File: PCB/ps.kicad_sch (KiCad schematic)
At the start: 8 parts, among them J2 Power

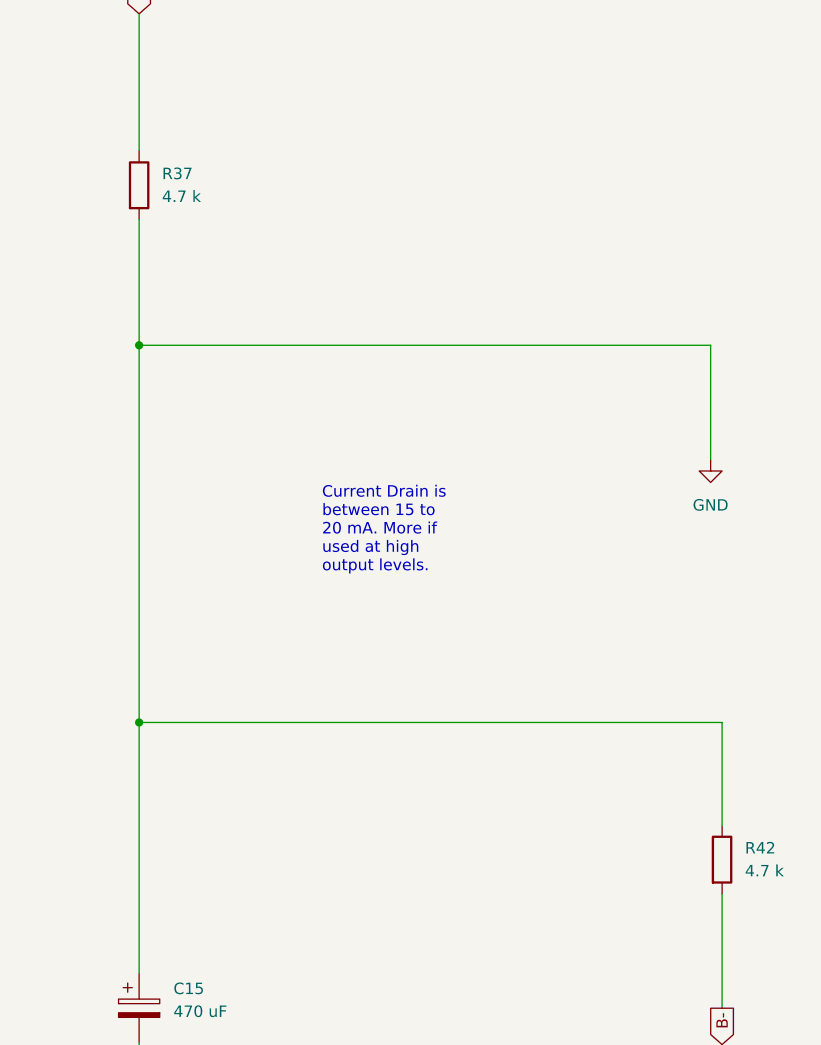
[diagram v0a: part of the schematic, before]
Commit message: Change TO-92 transistors to wide package to avoid shorting during soldering
Added B- hole for speaker
Added more vias to shorten traces
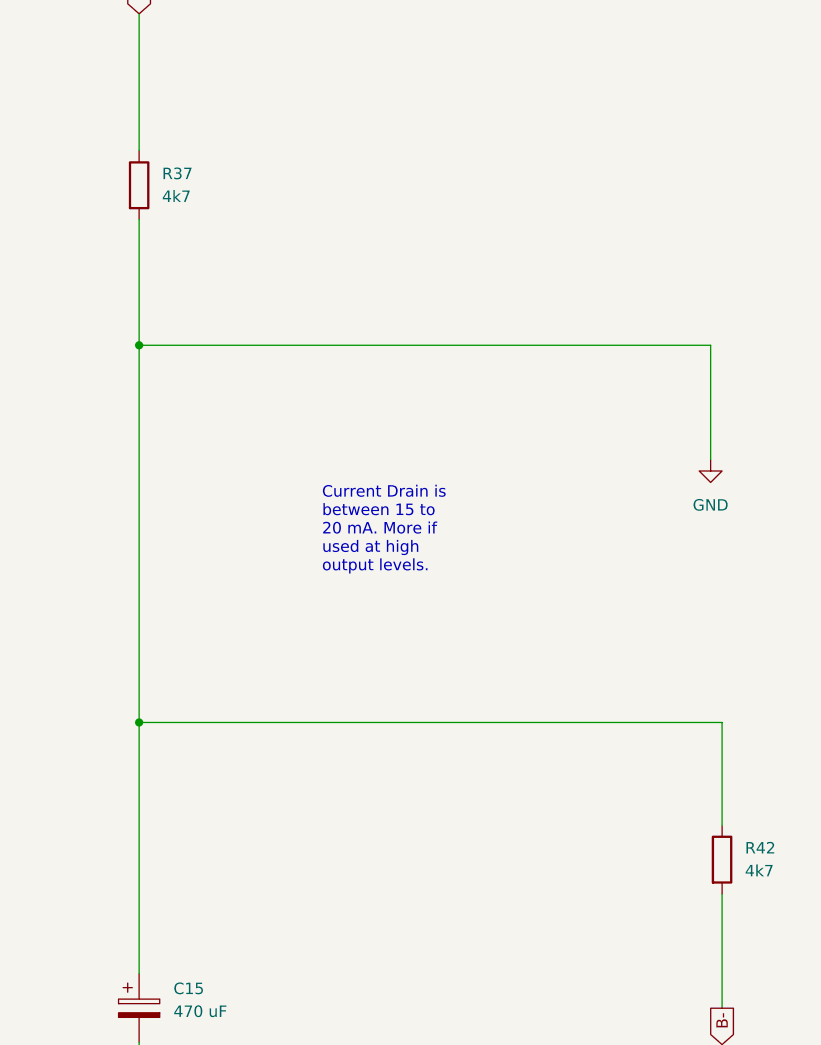
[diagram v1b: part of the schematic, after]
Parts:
- R37, R42: value 4.7 k -> 4k7
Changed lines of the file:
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@@
 		(fields_autoplaced yes)
 		(property "Reference" "R42"
-			(at 227.33 119.38 0)
-			(show_name no)
-			(do_not_autoplace no)
-			(effects
-				(font
-					(size 1.27 1.27)
-				)
-				(justify left)
-			)
-		)
-		(property "Value" "4.7 k"
-			(at 227.33 121.92 0)
+			(at 227.33 119.3799 0)
+			(show_name no)
+			(do_not_autoplace no)
+			(effects
+				(font
+					(size 1.27 1.27)
+				)
+				(justify left)
+			)
+		)
+		(property "Value" "4k7"
+			(at 227.33 121.9199 0)
 			(show_name no)
 			(do_not_autoplace no)
@@
 		(fields_autoplaced yes)
 		(property "Reference" "R37"
-			(at 162.56 44.45 0)
-			(show_name no)
-			(do_not_autoplace no)
-			(effects
-				(font
-					(size 1.27 1.27)
-				)
-				(justify left)
-			)
-		)
-		(property "Value" "4.7 k"
-			(at 162.56 46.99 0)
-			(show_name no)
-			(do_not_autoplace no)
+			(at 162.56 44.4499 0)
+			(show_name no)
+			(do_not_autoplace no)
+			(effects
+				(font
+					(size 1.27 1.27)
+				)
+				(justify left)
+			)
+		)
+		(property "Value" "4k7"
+			(at 162.56 46.9899 0)
+			(show_name no)
+			(do_not_autoplace no)

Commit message: Necessary Changes to Schematic and PCB
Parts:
- C13, C14: footprint Capacitor_THT:CP_Radial_D4.0mm_P1.50mm -> Capacitor_THT:CP_Radial_D4.0mm_P2.00mm
- C15, C23: footprint Capacitor_THT:CP_Radial_D14.0mm_P5.00mm -> Capacitor_THT:CP_Radial_D10.0mm_P5.00mm
- J10: renamed from GND1; footprint Connector_PinHeader_2.00mm:PinHeader_1x01_P2.00mm_Vertical -> Connector_PinSocket_2.54mm:PinSocket_1x04_P2.54mm_Vertical; symbol Connector:Conn_01x01_Pin -> Connector:Conn_01x04_Pin
- J2: footprint Connector_PinHeader_2.00mm:PinHeader_1x02_P2.00mm_Vertical -> Connector_PinSocket_2.54mm:PinSocket_1x02_P2.54mm_Vertical
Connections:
- net GND: now also J10.2 (Pin_2), J10.3 (Pin_3), J10.4 (Pin_4)
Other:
- note added: "Virtual Ground"
- note removed: "Virual Ground"
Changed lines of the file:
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@@
 		)
 	)
-	(text "Virual Ground\n"
+	(text "Virtual Ground\n"
 		(exclude_from_sim no)
 		(at 114.3 115.57 0)
@@
 	)
 	(junction
+		(at 127 101.6)
+		(diameter 0)
+		(color 0 0 0 0)
+	)
+	(junction
+		(at 127 104.14)
+		(diameter 0)
+		(color 0 0 0 0)
+	)
+	(junction
 		(at 160.02 63.5)
 		(diameter 0)
@@
 	(wire
 		(pts
+			(xy 127 101.6) (xy 127 104.14)
+		)
+		(stroke
+			(width 0)
+			(type default)
+		)
+	)
+	(wire
+		(pts
 			(xy 120.65 104.14) (xy 127 104.14)
 		)
@@
 	(wire
 		(pts
+			(xy 127 104.14) (xy 127 106.68)
+		)
+		(stroke
+			(width 0)
+			(type default)
+		)
+	)
+	(wire
+		(pts
 			(xy 160.02 26.67) (xy 160.02 41.91)
 		)
@@
 		(pts
 			(xy 120.65 106.68) (xy 120.65 104.14)
+		)
+		(stroke
+			(width 0)
+			(type default)
+		)
+	)
+	(wire
+		(pts
+			(xy 127 99.06) (xy 127 101.6)
 		)
 		(stroke
@@
 			)
 		)
-		(property "Footprint" "Capacitor_THT:CP_Radial_D14.0mm_P5.00mm"
+		(property "Footprint" "Capacitor_THT:CP_Radial_D10.0mm_P5.00mm"
 			(at 60.6552 105.41 0)
 			(hide yes)
@@
 			)
 		)
-		(property "Footprint" "Capacitor_THT:CP_Radial_D14.0mm_P5.00mm"
+		(property "Footprint" "Capacitor_THT:CP_Radial_D10.0mm_P5.00mm"
 			(at 160.9852 140.97 0)
 			(hide yes)
@@
 	)
 	(symbol
-		(lib_id "Connector:Conn_01x01_Pin")
+		(lib_id "Connector:Conn_01x04_Pin")
 		(at 132.08 104.14 180)
 		(unit 1)
@@
 		(in_pos_files yes)
 		(dnp no)
-		(property "Reference" "GND1"
+		(property "Reference" "J10"
 			(at 130.81 107.95 0)
 			(hide yes)
@@
 		)
 		(property "Value" "GND"
-			(at 129.54 100.33 0)
-			(show_name no)
-			(do_not_autoplace no)
-			(effects
-				(font
-					(size 1.27 1.27)
-				)
-			)
-		)
-		(property "Footprint" "Connector_PinHeader_2.00mm:PinHeader_1x01_P2.00mm_Vertical"
+			(at 135.382 100.584 0)
+			(hide yes)
+			(show_name no)
+			(do_not_autoplace no)
+			(effects
+				(font
+					(size 1.27 1.27)
+				)
+			)
+		)
+		(property "Footprint" "Connector_PinSocket_2.54mm:PinSocket_1x04_P2.54mm_Vertical"
 			(at 132.08 104.14 0)
 			(hide yes)
@@
 			)
 		)
-		(property "Description" ""
+		(property "Description" "Generic connector, single row, 01x04, script generated"
 			(at 132.08 104.14 0)
 			(hide yes)
@@
 		)
 		(pin "1"
+		)
+		(pin "4"
+		)
+		(pin "3"
+		)
+		(pin "2"
 		)
 		(instances
 			(project "Noise Toaster PCB"
 				(path "/7be3f398-d902-4566-9ee4-0bff072cd47e/8163954c-0389-42ef-b929-449d078595e3"
-					(reference "GND1")
+					(reference "J10")
 					(unit 1)
 				)
@@
 			)
 		)
-		(property "Footprint" "Capacitor_THT:CP_Radial_D4.0mm_P1.50mm"
+		(property "Footprint" "Capacitor_THT:CP_Radial_D4.0mm_P2.00mm"
 			(at 106.3752 83.82 0)
 			(hide yes)
@@
 			)
 		)
-		(property "Footprint" "Connector_PinHeader_2.00mm:PinHeader_1x02_P2.00mm_Vertical"
+		(property "Footprint" "Connector_PinSocket_2.54mm:PinSocket_1x02_P2.54mm_Vertical"
 			(at 38.1 100.33 0)
 			(hide yes)
@@
 			)
 		)
-		(property "Footprint" "Capacitor_THT:CP_Radial_D4.0mm_P1.50mm"
+		(property "Footprint" "Capacitor_THT:CP_Radial_D4.0mm_P2.00mm"
 			(at 106.3752 133.35 0)
 			(hide yes)

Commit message: Fixed grave mistake (Q10 position swapped)
Tom forgot to mirror Q10, swapping the emitter and collectors of Q10
Changed all the footprints of electrolytic caps to 5mm (i didnt find a single cap in my parts bin rated for 25V that was 4mm diameter)
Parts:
- C13, C14: footprint Capacitor_THT:CP_Radial_D4.0mm_P2.00mm -> Capacitor_THT:CP_Radial_D5.0mm_P2.00mm
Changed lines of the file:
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@@
 			)
 		)
-		(property "Footprint" "Capacitor_THT:CP_Radial_D4.0mm_P2.00mm"
+		(property "Footprint" "Capacitor_THT:CP_Radial_D5.0mm_P2.00mm"
 			(at 106.3752 83.82 0)
 			(hide yes)
@@
 			)
 		)
-		(property "Footprint" "Capacitor_THT:CP_Radial_D4.0mm_P2.00mm"
+		(property "Footprint" "Capacitor_THT:CP_Radial_D5.0mm_P2.00mm"
 			(at 106.3752 133.35 0)
 			(hide yes)
